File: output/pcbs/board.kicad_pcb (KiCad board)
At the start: 2 copper layers, 141.8 x 108.1 mm, 40 parts

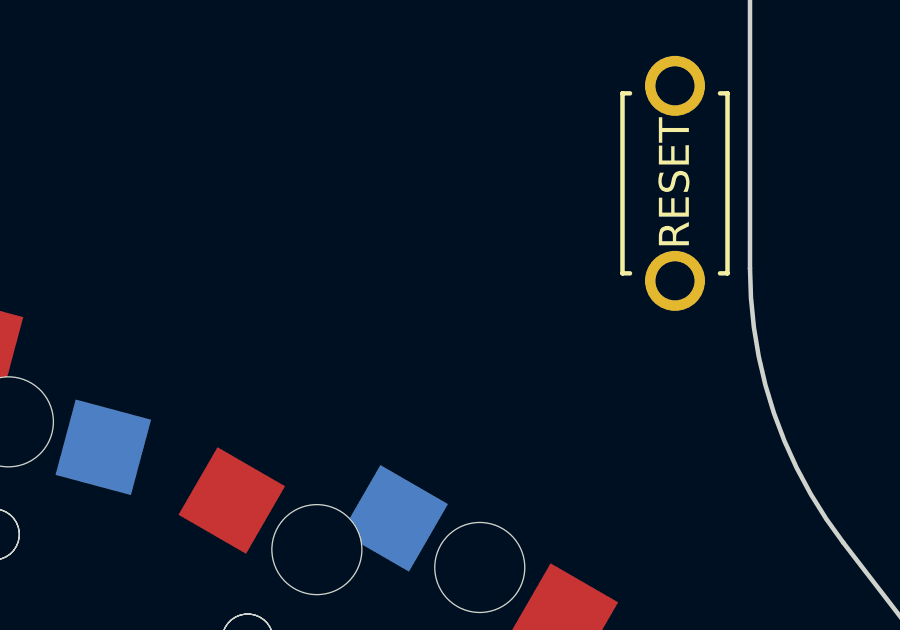
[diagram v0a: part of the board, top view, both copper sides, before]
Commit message: Adding battery footprint, and pointing to my new ergogen fork.
Still require routing.
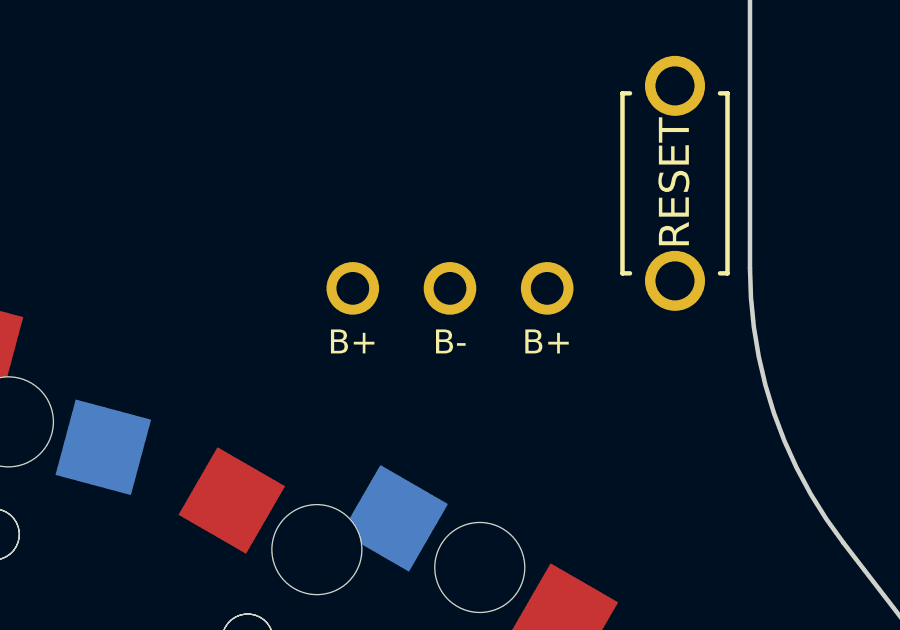
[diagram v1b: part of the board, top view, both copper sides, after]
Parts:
- added PAD1: , lib:bat, F.Cu at (106.1, -0.40)
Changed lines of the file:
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@@
             (pad "" smd rect (at -3.7 -1.1 270) (size 0.9 0.9) (layers B.Cu B.Paste B.Mask))
         )
+            (module lib:bat (layer F.Cu)
+                (at 106.06786 -0.39742239999999995 0)
+                (fp_text reference "PAD1" (at 0 0) (layer F.SilkS) hide (effects (font (size 1.27 1.27) (thickness 0.15))))
+                (fp_text value "" (at 0 0) (layer F.SilkS) hide (effects (font (size 1.27 1.27) (thickness 0.15))))
+                (fp_text user "B+" (at -3.24 1.8 0) (layer F.SilkS) (effects (font (size 0.8 0.8) (thickness 0.15)) ))
+                (fp_text user "B+" (at -3.24 1.8 0) (layer B.SilkS) (effects (font (size 0.8 0.8) (thickness 0.15)) (justify mirror)))
+                (pad 1 thru_hole circle (at -3.24 0 0) (size 1.7526 1.7526) (drill 1.0922) (layers *.Cu *.SilkS *.Mask) (net 25 "Braw"))
+                (fp_text user "B-" (at 0 1.8 0) (layer F.SilkS) (effects (font (size 0.8 0.8) (thickness 0.15)) ))
+                (fp_text user "B-" (at 0 1.8 0) (layer B.SilkS) (effects (font (size 0.8 0.8) (thickness 0.15)) (justify mirror)))
+                (pad 1 thru_hole circle (at 0 0 0) (size 1.7526 1.7526) (drill 1.0922) (layers *.Cu *.SilkS *.Mask) (net 24 "Bminus"))
+                (fp_text user "B+" (at 3.24 1.8 0) (layer F.SilkS) (effects (font (size 0.8 0.8) (thickness 0.15)) ))
+                (fp_text user "B+" (at 3.24 1.8 0) (layer B.SilkS) (effects (font (size 0.8 0.8) (thickness 0.15)) (justify mirror)))
+                (pad 1 thru_hole circle (at 3.24 0 0) (size 1.7526 1.7526) (drill 1.0922) (layers *.Cu *.SilkS *.Mask) (net 25 "Braw"))
+            )
             (module kbd:ResetSW (layer F.Cu)
                 (descr "Two pin through hole Tactile Switch, the same as on the Corne")

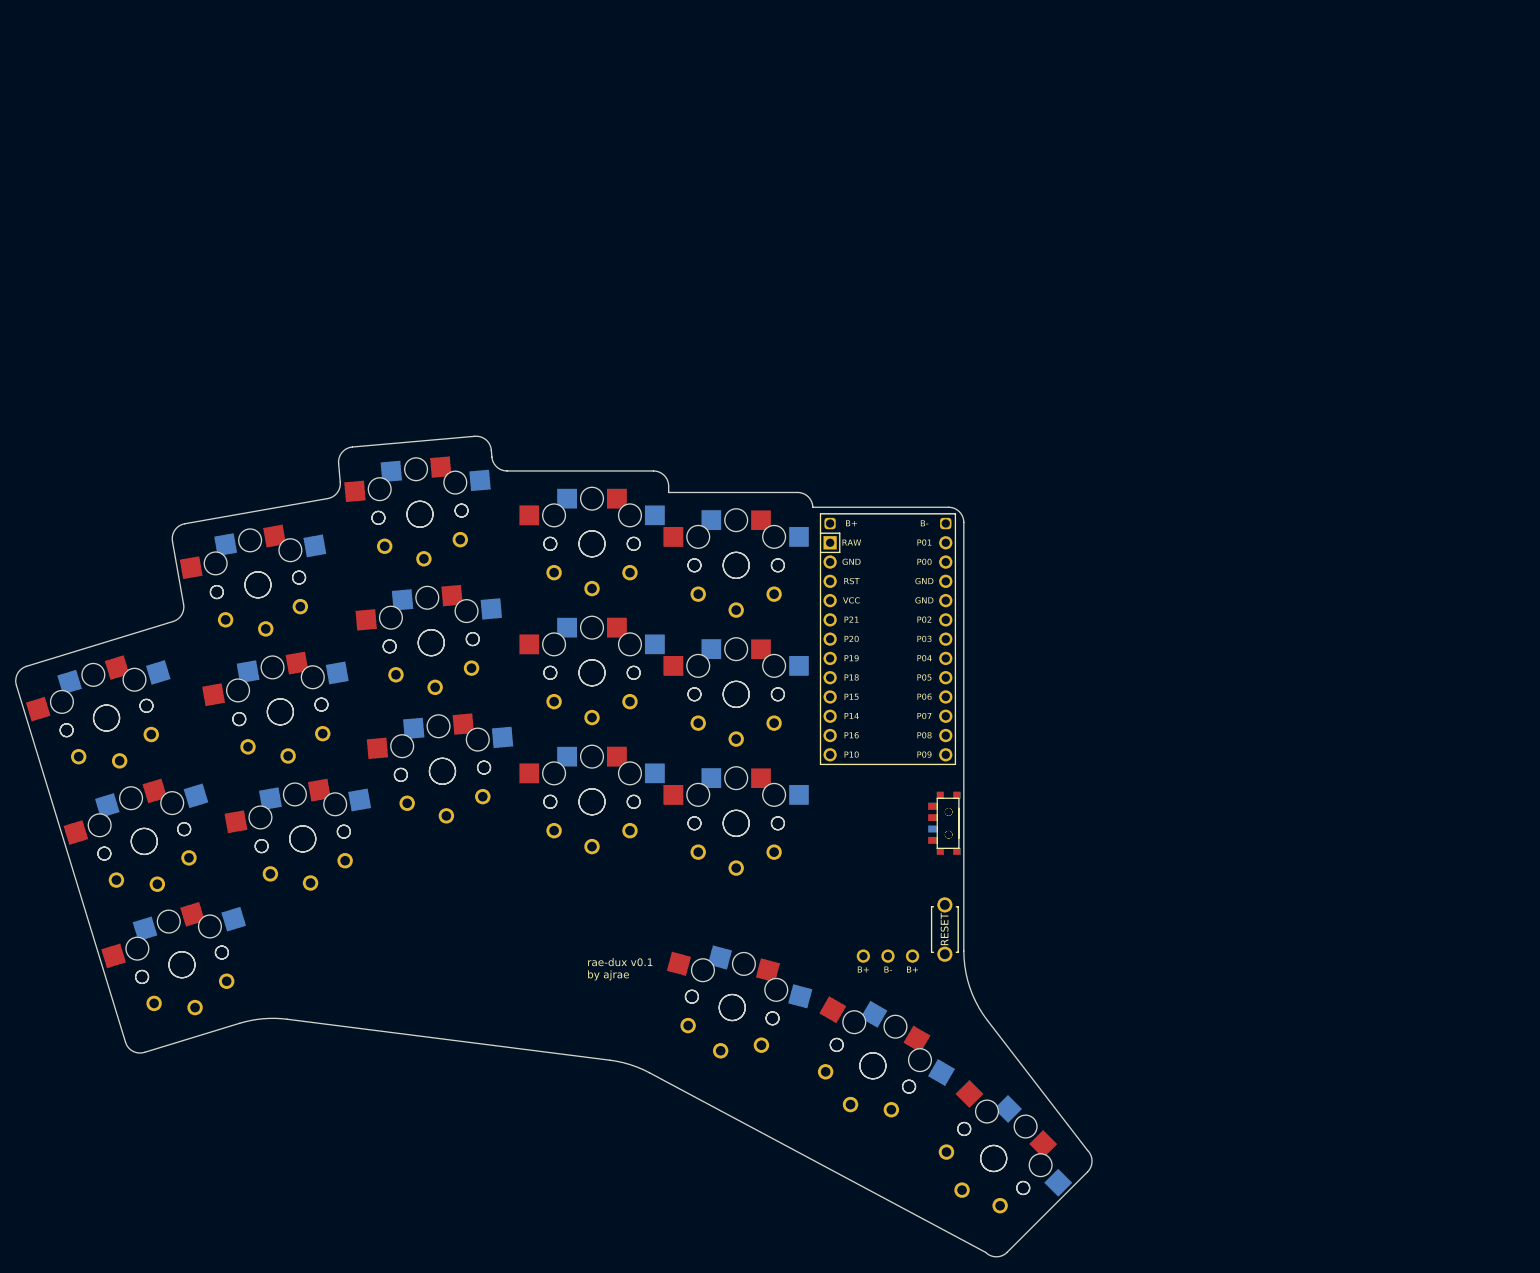
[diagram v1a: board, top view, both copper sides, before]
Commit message: Routed new design with battery connectors.
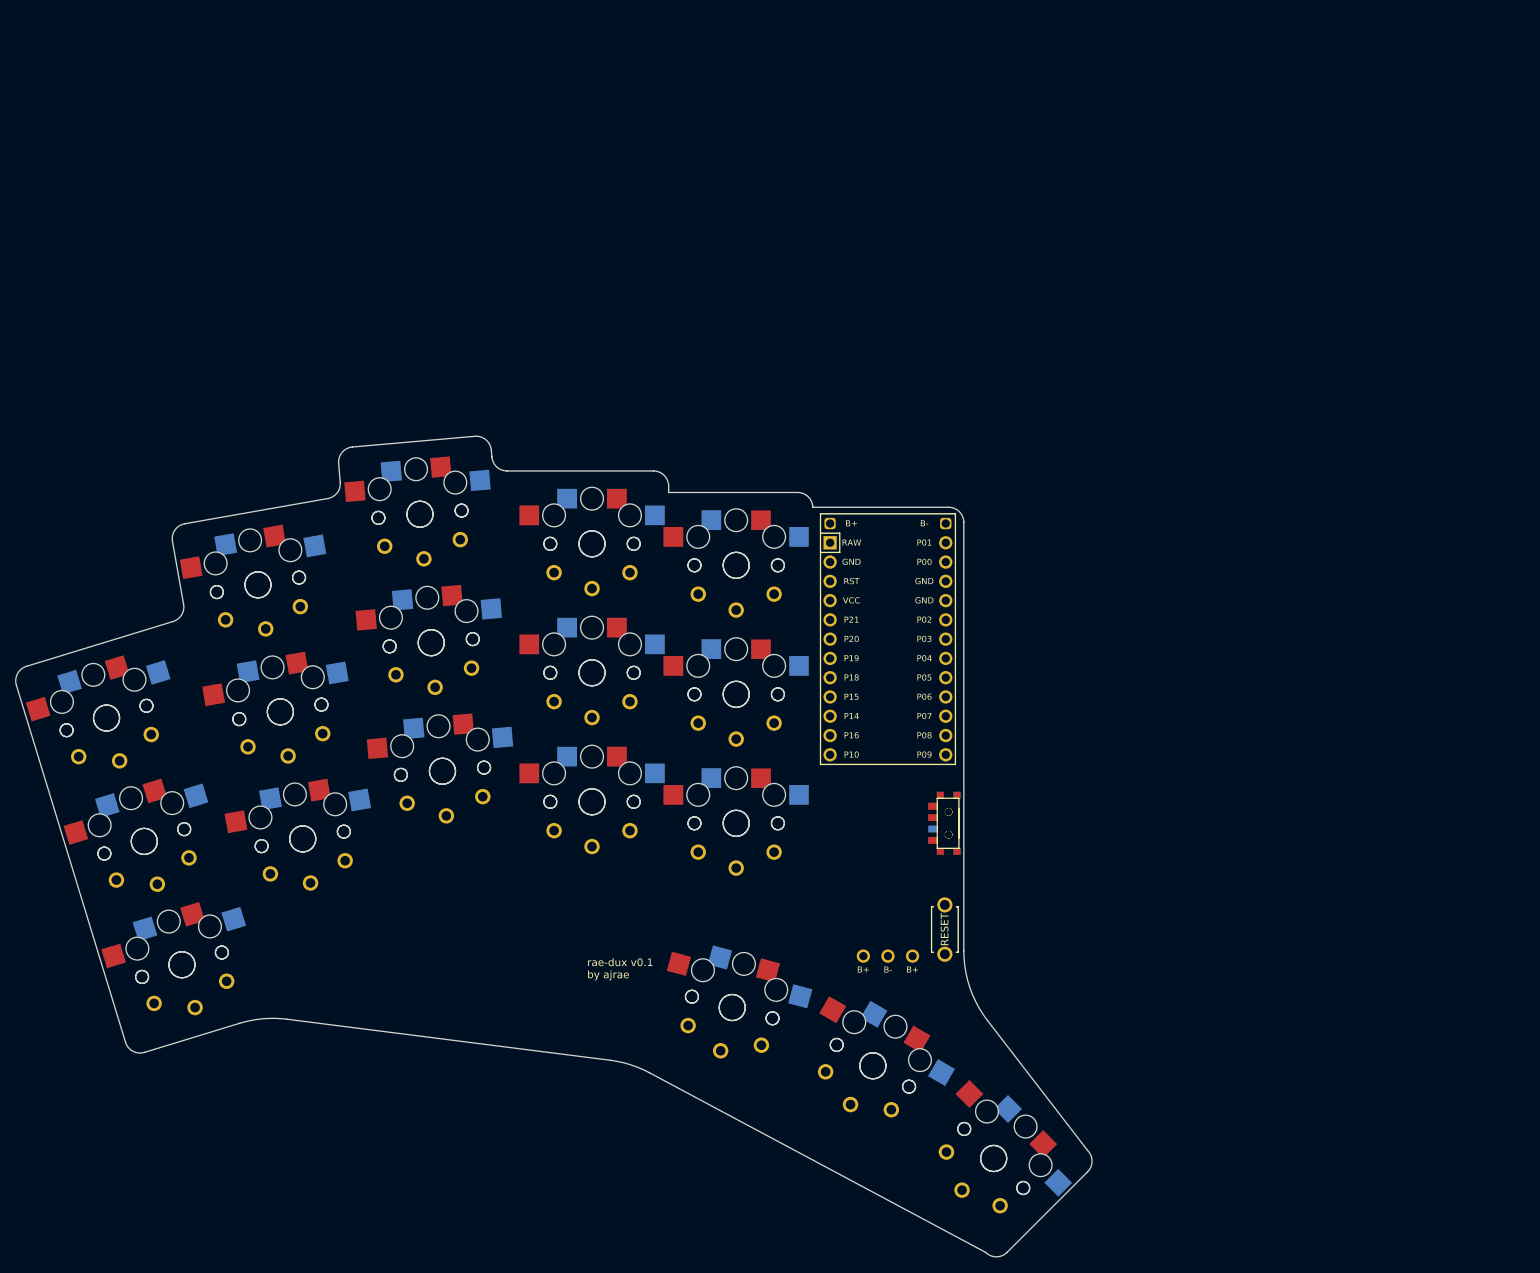
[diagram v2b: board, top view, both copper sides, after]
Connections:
- MCU1 pad 25: Bminus -> Bplus
- S15 pad 1: P10 -> P18
- S16 pad 1: P10 -> P18
- S17 pad 1: P16 -> P15
- S18 pad 1: P16 -> P15
- S21 pad 1: P15 -> P16
- S22 pad 1: P15 -> P16
- S23 pad 1: P18 -> P10
- S24 pad 1: P18 -> P10
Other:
- net class Default removed
- net class Power removed

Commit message: Increasing pinky stagger and fixing battery footprint to actually work with JST PH (fixed upstream in ergogen fork).
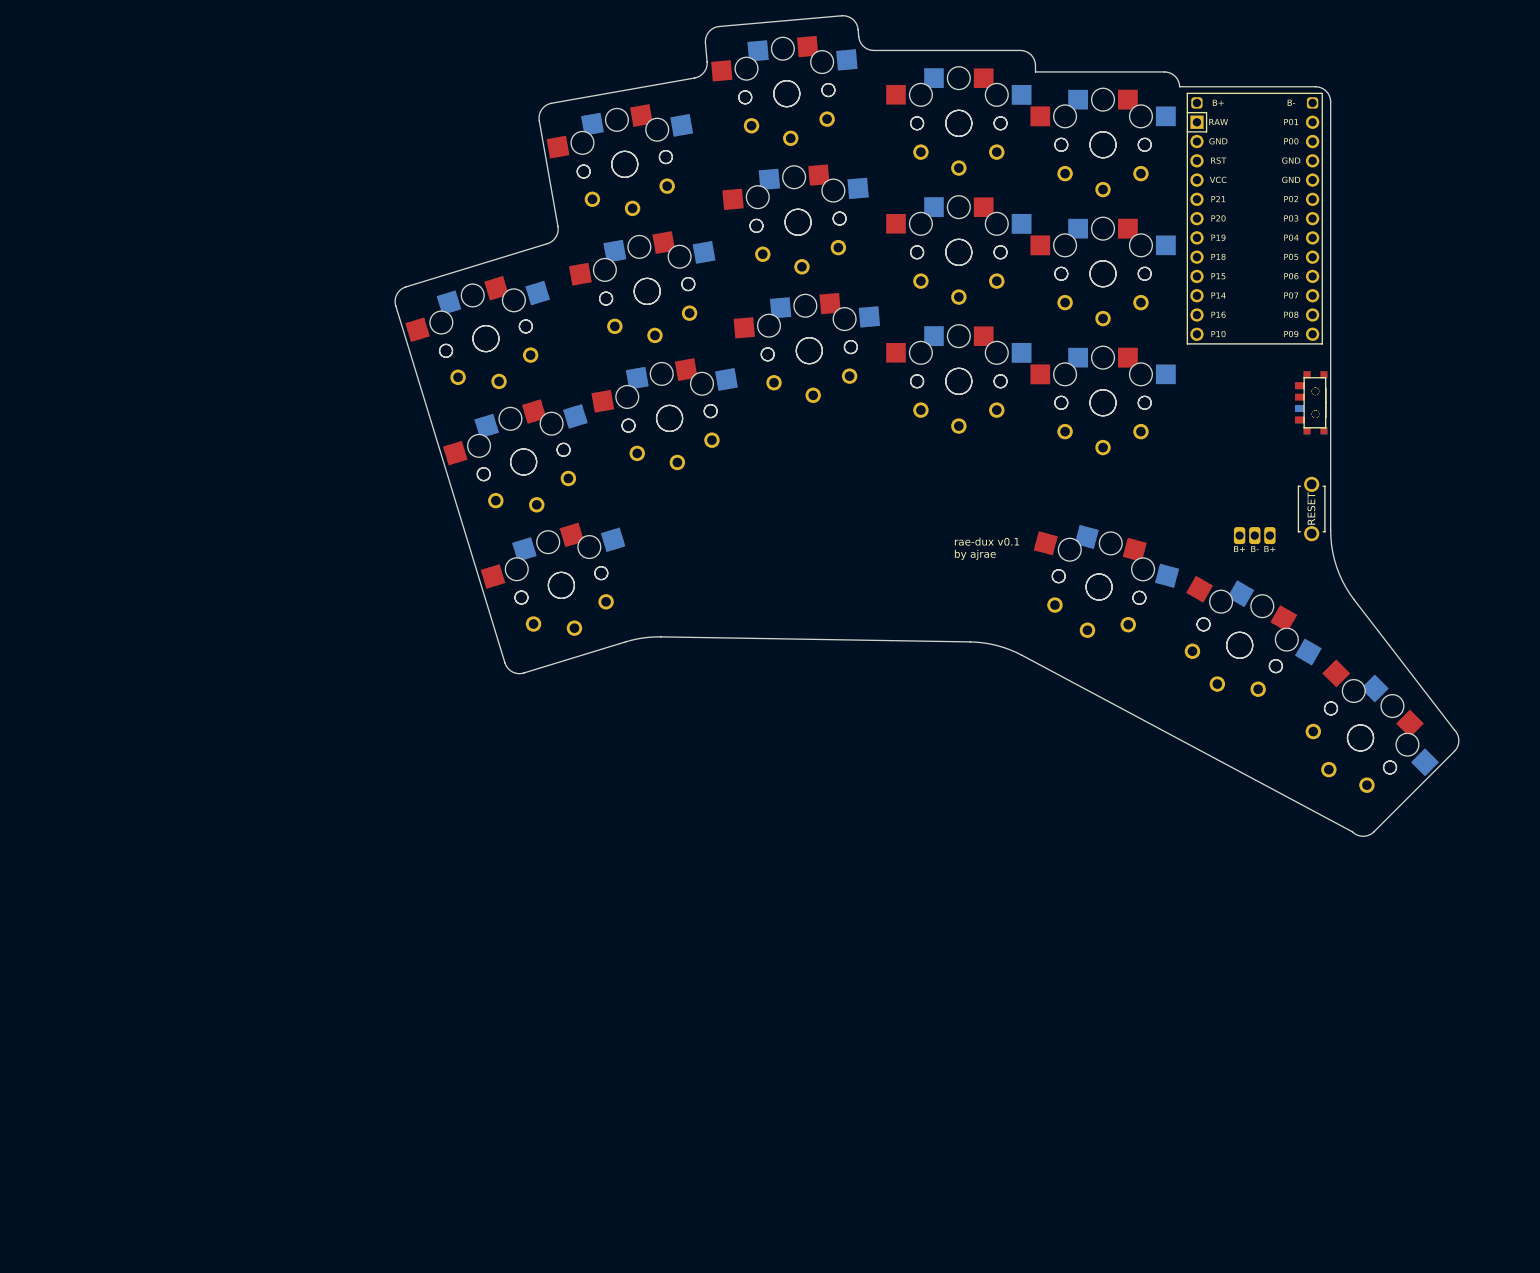
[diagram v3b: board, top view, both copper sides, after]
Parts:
- moved B1 73.5 mm to (161.9, -59.3)
- moved PAD1 73.5 mm to (154.4, -55.8)
- moved S25 73.5 mm to (134.4, -73.3)
- moved S26 73.5 mm to (134.4, -73.3)
- moved T1 73.5 mm to (162.4, -73.3)
- moved T2 73.5 mm to (162.4, -73.3)
- moved S17 73.5 mm to (92.7, -114.0)
- moved S18 73.5 mm to (92.7, -114.0)
- moved S35 73.5 mm to (168.3, -29.1)
- moved S36 73.5 mm to (168.3, -29.1)
- moved S33 73.5 mm to (152.4, -41.4)
- moved S34 73.5 mm to (152.4, -41.4)
- moved S13 73.5 mm to (95.7, -80.2)
- moved S14 73.5 mm to (95.7, -80.2)
- moved S31 73.5 mm to (133.9, -49.0)
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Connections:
- MCU1 pad 25: Bplus -> Bminus
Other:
- board size 141.8 x 108.1 mm -> 140.2 x 108.1 mm
- net class Default added: clearance 0.2, trace_width 0.25, via_dia 0.8, via_drill 0.4
- net class Power added: clearance 0.2, trace_width 0.5, via_dia 0.8, via_drill 0.4

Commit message: add latest output
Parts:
- added G***: LOGO, LOGO, F.Cu at (104.5, -43.5)
- added G***: LOGO, LOGO, B.Cu at (104.5, -44.0)
- moved S17 17.1 mm to (104.2, -101.3), turned to 0 degrees
- moved S18 17.1 mm to (104.2, -101.3), turned to 180 degrees
- moved S11 16.7 mm to (86.0, -96.6), turned to 0 degrees
- moved S12 16.7 mm to (86.0, -96.6), turned to 180 degrees
- moved S15 16.2 mm to (104.2, -84.3), turned to 0 degrees
- moved S16 16.2 mm to (104.2, -84.3), turned to 180 degrees
- moved S13 15.4 mm to (104.2, -67.3), turned to 0 degrees
- moved S14 15.4 mm to (104.2, -67.3), turned to 180 degrees
- moved S27 15.1 mm to (141.0, -76.7)
- moved S28 15.1 mm to (141.0, -76.7)
- moved MCU1 15.1 mm to (161.0, -82.7)
- moved S29 15.1 mm to (141.0, -93.7)
- moved S30 15.1 mm to (141.0, -93.7)
- moved B1 15.1 mm to (168.5, -45.7)
- moved S25 15.1 mm to (141.0, -59.7)
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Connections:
- MCU1 pad 13: P1 -> P9
- MCU1 pad 14: P0 -> P8
- MCU1 pad 15: GND -> P7
- MCU1 pad 16: GND -> P6
- MCU1 pad 17: P2 -> P5
- MCU1 pad 18: P3 -> P4
- MCU1 pad 19: P4 -> P3
- MCU1 pad 20: P5 -> P2
- MCU1 pad 21: P6 -> GND
- MCU1 pad 22: P7 -> GND
- MCU1 pad 23: P8 -> P0
- MCU1 pad 24: P9 -> P1
- S15 pad 1: P18 -> P16
- S16 pad 1: P18 -> P16
- S17 pad 1: P15 -> P10
- S18 pad 1: P15 -> P10
- S21 pad 1: P16 -> P15
- S22 pad 1: P16 -> P15
- S23 pad 1: P10 -> P18
- S24 pad 1: P10 -> P18
- T1 pad 2: Bplus -> RAW
- T2 pad 2: Bplus -> RAW
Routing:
- net P0: track 0.00 -> 185.5 mm
- net P4: track 0.00 -> 177.4 mm
- net P2: track 0.00 -> 160.7 mm
- net P5: track 0.00 -> 159.4 mm
- net P10: track 0.00 -> 152.7 mm
- net P6: track 0.00 -> 147.5 mm
- net P3: track 0.00 -> 143.8 mm
- net P1: track 0.00 -> 140.2 mm
- net P16: track 0.00 -> 136.4 mm
- net P18: track 0.00 -> 132.7 mm
- net P15: track 0.00 -> 111.2 mm
- net P14: track 0.00 -> 99.4 mm
- net P9: track 0.00 -> 87.2 mm
- net P8: track 0.00 -> 79.4 mm
- net P7: track 0.00 -> 72.6 mm
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- added copper zone on B.Cu, net GND
- added copper zone on F.Cu, net GND
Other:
- board size 140.2 x 108.1 mm -> 131.4 x 98.8 mm
- net class Default removed
- net class Power removed
- board text added: "DNA sweep v1.0"
- board text removed: "rae-dux v0.1 by ajrae"
